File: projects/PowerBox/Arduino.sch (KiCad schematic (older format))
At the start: 51 parts, among them CON3 USB-MINI-B-Vert, IC3 LM358, P11 CONN_10, P12 CONN_8, P13 CONN_8, P14 CONN_6, P7 ICSP, Q4 DMG3415U, Q5 DMG3415U, U4 INA219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

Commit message: digikey partnumbers in schematic added
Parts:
- D12: DK (none) -> 568-6472-1-ND
- IC3: DK (none) -> LM358MXFSCT-ND
- Q4, Q5: DK (none) -> DMG3415UDICT-ND
- R28: DK (none) -> P.10AUCT-ND
- R31, R32, R33, R34: DK (none) -> P220CCT-ND
- VR1, VR2: DK (none) -> 478-5584-1-ND
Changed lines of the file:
@@
 F 2 "frep:R0805" V 1630 6550 30  0001 C CNN
 F 3 "" H 1700 6550 30  0000 C CNN
+F 4 "P220CCT-ND" V 1700 6550 60  0001 C CNN "DK"
 	1    1700 6550
 	-1   0    0    1
@@
 F 2 "frep:R0805" V 1330 6550 30  0001 C CNN
 F 3 "" H 1400 6550 30  0000 C CNN
+F 4 "P220CCT-ND" V 1400 6550 60  0001 C CNN "DK"
 	1    1400 6550
 	-1   0    0    1
@@
 F 2 "frep:R0805" V 1030 6550 30  0001 C CNN
 F 3 "" H 1100 6550 30  0000 C CNN
+F 4 "P220CCT-ND" V 1100 6550 60  0001 C CNN "DK"
 	1    1100 6550
 	-1   0    0    1
@@
 F 2 "frep:R0805" V 1930 6550 30  0001 C CNN
 F 3 "" H 2000 6550 30  0000 C CNN
+F 4 "P220CCT-ND" V 2000 6550 60  0001 C CNN "DK"
 	1    2000 6550
 	-1   0    0    1
@@
 F 2 "frep:SOIC8" H 5650 2250 50  0001 C CNN
 F 3 "" H 5650 2100 60  0000 C CNN
+F 4 "LM358MXFSCT-ND" H 5650 2100 60  0001 C CNN "DK"
 	1    5650 2100
 	1    0    0    -1
@@
 F 2 "frep:SOIC8" H 5750 1650 50  0001 C CNN
 F 3 "" H 5750 1500 60  0000 C CNN
+F 4 "LM358MXFSCT-ND" H 5750 1500 60  0001 C CNN "DK"
 	2    5750 1500
 	1    0    0    1
@@
 F 2 "frep:SOT23" V 6650 2400 50  0001 C CNN
 F 3 "" V 6500 2400 60  0000 C CNN
+F 4 "DMG3415UDICT-ND" H 6500 2400 60  0001 C CNN "DK"
 	1    6500 2400
 	-1   0    0    -1
@@
 F 2 "frep:R1206" V 5280 6700 30  0001 C CNN
 F 3 "" H 5350 6700 30  0000 C CNN
+F 4 "P.10AUCT-ND" V 5350 6700 60  0001 C CNN "DK"
 	1    5350 6700
 	1    0    0    -1
@@
 F 2 "frep:SOT23" V 7050 1500 50  0001 C CNN
 F 3 "" V 6900 1500 60  0000 C CNN
+F 4 "DMG3415UDICT-ND" H 6900 1500 60  0001 C CNN "DK"
 	1    6900 1500
 	0    -1   -1   0
@@
 F 2 "frep:R0805" H 2000 3250 60  0001 C CNN
 F 3 "" H 2000 3250 60  0000 C CNN
+F 4 "478-5584-1-ND" V 2000 3250 60  0001 C CNN "DK"
 	1    2000 3250
 	1    0    0    -1
@@
 F 2 "frep:R0805" H 2300 3250 60  0001 C CNN
 F 3 "" H 2300 3250 60  0000 C CNN
+F 4 "478-5584-1-ND" V 2300 3250 60  0001 C CNN "DK"
 	1    2300 3250
 	1    0    0    -1
@@
 F 2 "frep:SOT23" H 3500 2900 60  0001 C CNN
 F 3 "" H 3500 2900 60  0000 C CNN
+F 4 "568-6472-1-ND" H 3500 2900 60  0001 C CNN "DK"
 	1    3500 2900
 	0    -1   -1   0

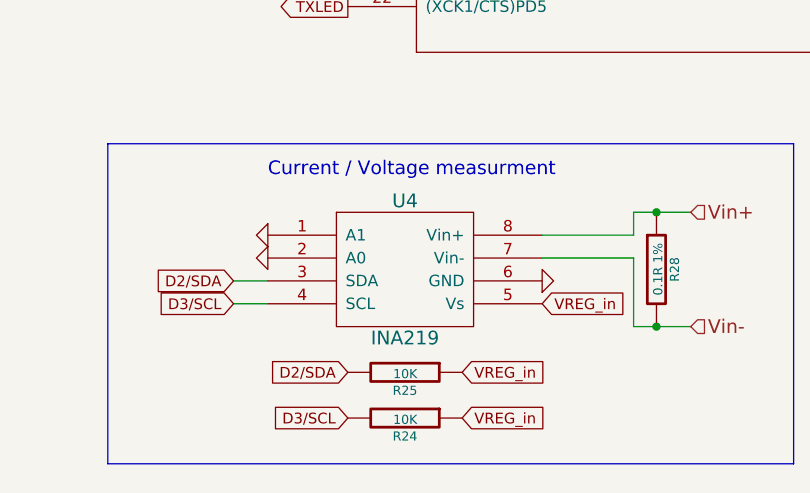
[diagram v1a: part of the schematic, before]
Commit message: ina219 footprint and pin-assignement changed
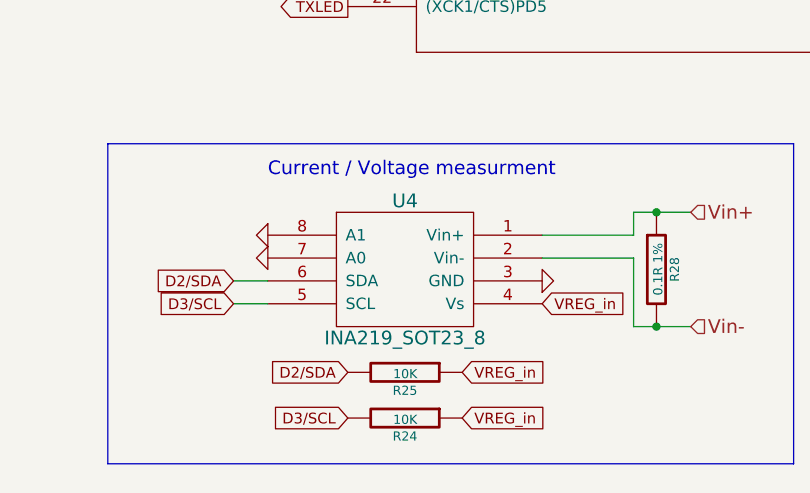
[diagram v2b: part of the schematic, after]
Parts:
- removed U4: INA219, frep:SOIC8, symbol INA219
- added U4: INA219_SOT23_8, frep:SOT-23-8, symbol INA219_SOT23_8
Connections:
- net D2/SDA: now also U4.6 (SDA)
- net D3/SCL: now also U4.5 (SCL)
- net GND: now also U4.3 (GND), U4.7 (A0), U4.8 (A1)
- net VREG_in: now also U4.4 (Vs)
- net Vin+: now also U4.1 (Vin+)
- net Vin-: now also U4.2 (Vin-)
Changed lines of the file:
@@
 Text HLabel 1350 1550 0    60   Output ~ 0
 Latch
-$Comp
-L INA219 U4
-U 1 1 558FD6AF
-P 4250 6700
-F 0 "U4" H 4250 7000 60  0000 C CNN
-F 1 "INA219" H 4250 6400 60  0000 C CNN
-F 2 "frep:SOIC8" H 4250 6500 60  0001 C CNN
-F 3 "" H 4250 6500 60  0000 C CNN
-	1    4250 6700
-	1    0    0    -1
-$EndComp
 Text Notes 4900 2725 0    60   ~ 0
 transistor is conducting, when Vgs < 0
@@
 Text GLabel 2450 1850 2    47   Input ~ 0
 A0
+$Comp
+L INA219_SOT23_8 U4
+U 1 1 55B14D79
+P 4250 6700
+F 0 "U4" H 4250 7000 60  0000 C CNN
+F 1 "INA219_SOT23_8" H 4250 6400 60  0000 C CNN
+F 2 "frep:SOT-23-8" H 4250 6500 60  0001 C CNN
+F 3 "" H 4250 6500 60  0000 C CNN
+	1    4250 6700
+	1    0    0    -1
+$EndComp
 $EndSCHEMATC
